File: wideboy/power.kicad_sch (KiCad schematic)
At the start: 19 parts, among them U3 PQ30RV21, U4 PQ05RF21, U5 PQ30RV21

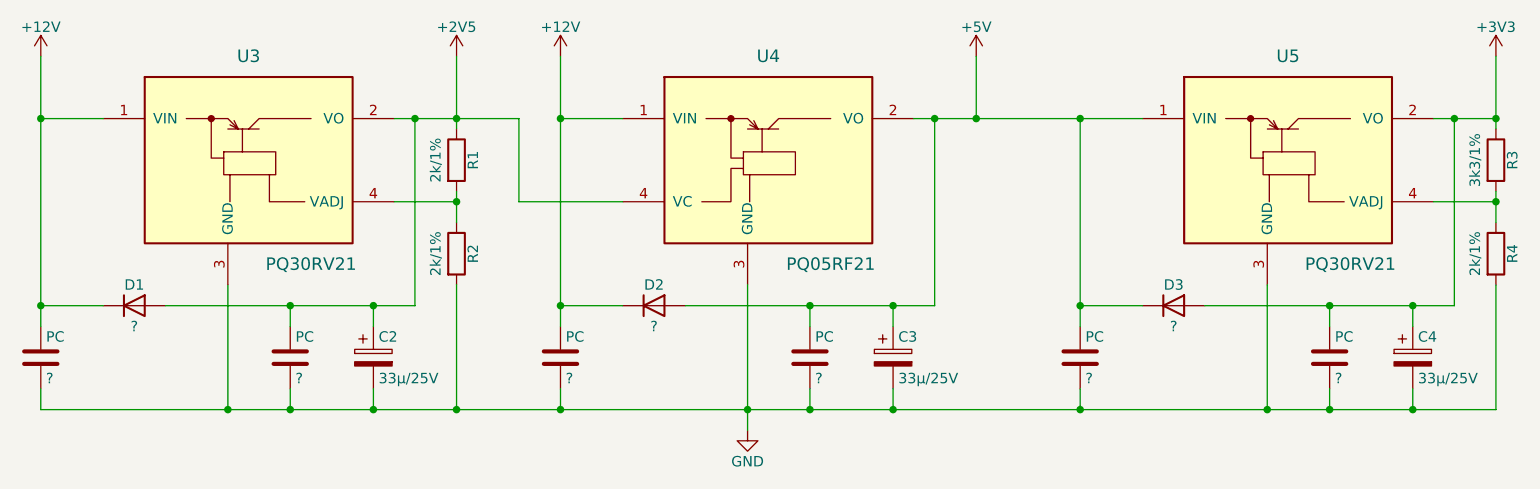
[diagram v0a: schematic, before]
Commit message: Add values for capacitors and diodes
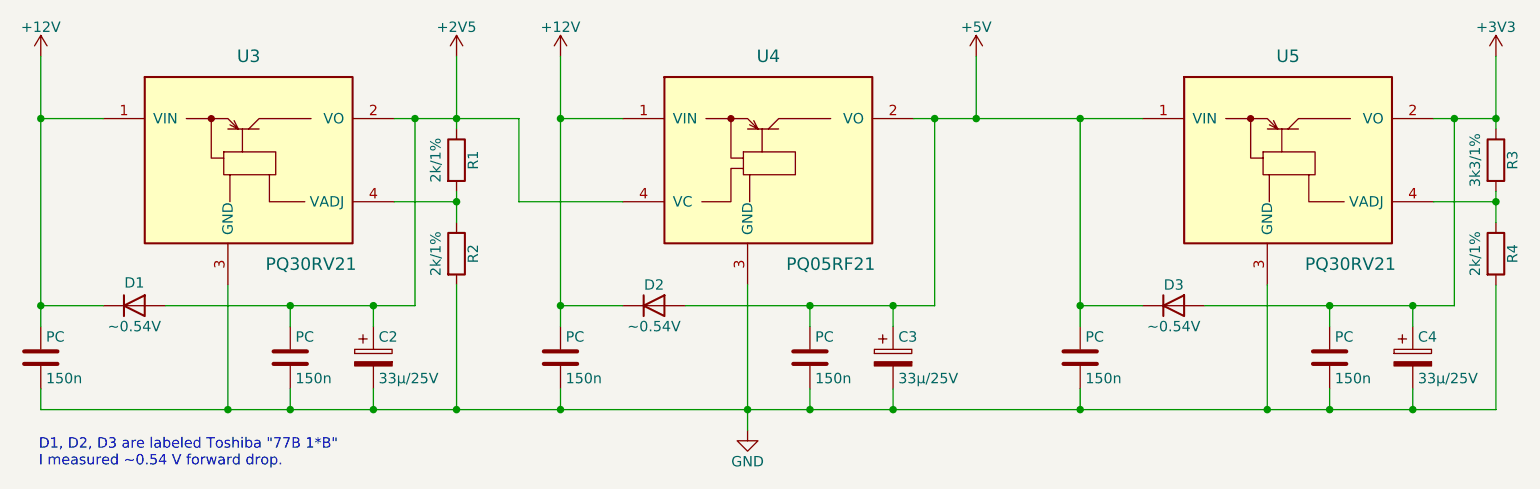
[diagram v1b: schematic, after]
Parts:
- D1, D2, D3: value ? -> ~0.54V
- PC: value ? -> 150n
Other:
- note added: "D1, D2, D3 are labeled Toshiba "77B 1*B" I measured ~0.54 V forward drop."
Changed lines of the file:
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@@
 	(title_block
 		(title "Wide-Boy64 AGB")
-		(date "2024-06-20")
-		(rev "2")
+		(date "2024-09-22")
+		(rev "3")
 		(company "CC-BY-SA-4.0 Michael Singer")
 		(comment 1 "https://github.com/msinger/wideboy/")
@@
 			(width 0)
 			(type default)
+		)
+	)
+	(text "D1, D2, D3 are labeled Toshiba \"77B 1*B\"\nI measured ~0.54 V forward drop."
+		(exclude_from_sim no)
+		(at 53.086 122.174 0)
+		(effects
+			(font
+				(size 1.27 1.27)
+			)
+			(justify left)
 		)
 	)
@@
 			)
 		)
-		(property "Value" "?"
+		(property "Value" "150n"
 			(at 53.975 113.03 0)
 			(effects
@@
 			)
 		)
-		(property "Value" "?"
+		(property "Value" "150n"
 			(at 84.455 113.03 0)
 			(effects
@@
 		(dnp no)
 		(property "Reference" "D1"
-			(at 64.77 101.6 0)
-			(effects
-				(font
-					(size 1.27 1.27)
-				)
-			)
-		)
-		(property "Value" "?"
+			(at 64.77 101.346 0)
+			(effects
+				(font
+					(size 1.27 1.27)
+				)
+			)
+		)
+		(property "Value" "~0.54V"
 			(at 64.77 106.68 0)
 			(effects
@@
 			)
 		)
-		(property "Value" "?"
+		(property "Value" "150n"
 			(at 117.475 113.03 0)
 			(effects
@@
 			)
 		)
-		(property "Value" "?"
+		(property "Value" "~0.54V"
 			(at 128.27 106.68 0)
 			(effects
@@
 			)
 		)
-		(property "Value" "?"
+		(property "Value" "150n"
 			(at 147.955 113.03 0)
 			(effects
@@
 			)
 		)
-		(property "Value" "?"
+		(property "Value" "150n"
 			(at 180.975 113.03 0)
 			(effects
@@
 			)
 		)
-		(property "Value" "?"
+		(property "Value" "~0.54V"
 			(at 191.77 106.68 0)
 			(effects
@@
 			)
 		)
-		(property "Value" "?"
+		(property "Value" "150n"
 			(at 211.455 113.03 0)
 			(effects
